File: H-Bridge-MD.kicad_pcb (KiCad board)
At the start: 2 copper layers, 85 x 50 mm, 70 parts, among them IC1 SI8650AB-B-IS1, IC2 AP7381-50SA-7, IC3 A3921KLPTR-T, IC4 SI8650AB-B-IS1, IC5 A3921KLPTR-T, J1 Conn_01x03, J2 Conn_01x05, J3 Bus_mechaken_PCIexpress_x16_1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, J4 Conn_01x02, J5 Conn_01x02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

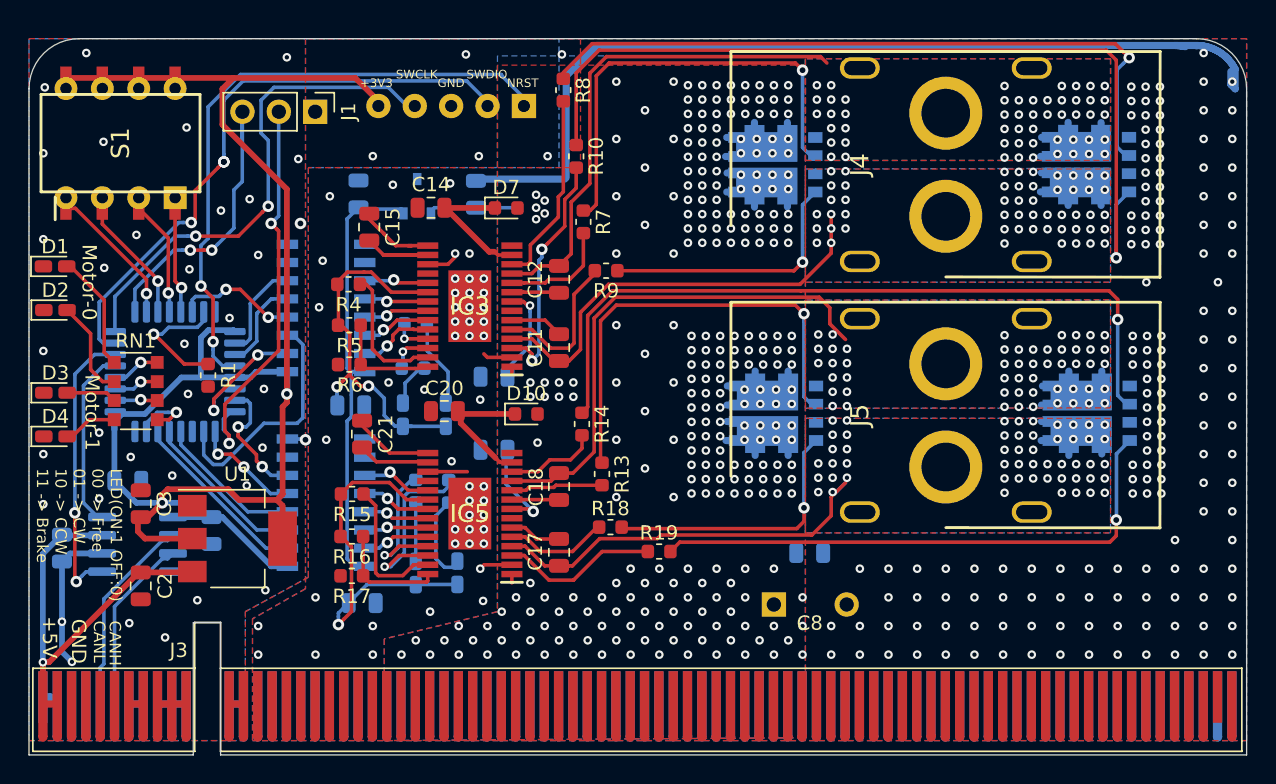
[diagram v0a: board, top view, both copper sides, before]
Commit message: change
エッジコネクタ（PCIe）を公式のライブラリを基にしたフットプリントに変更
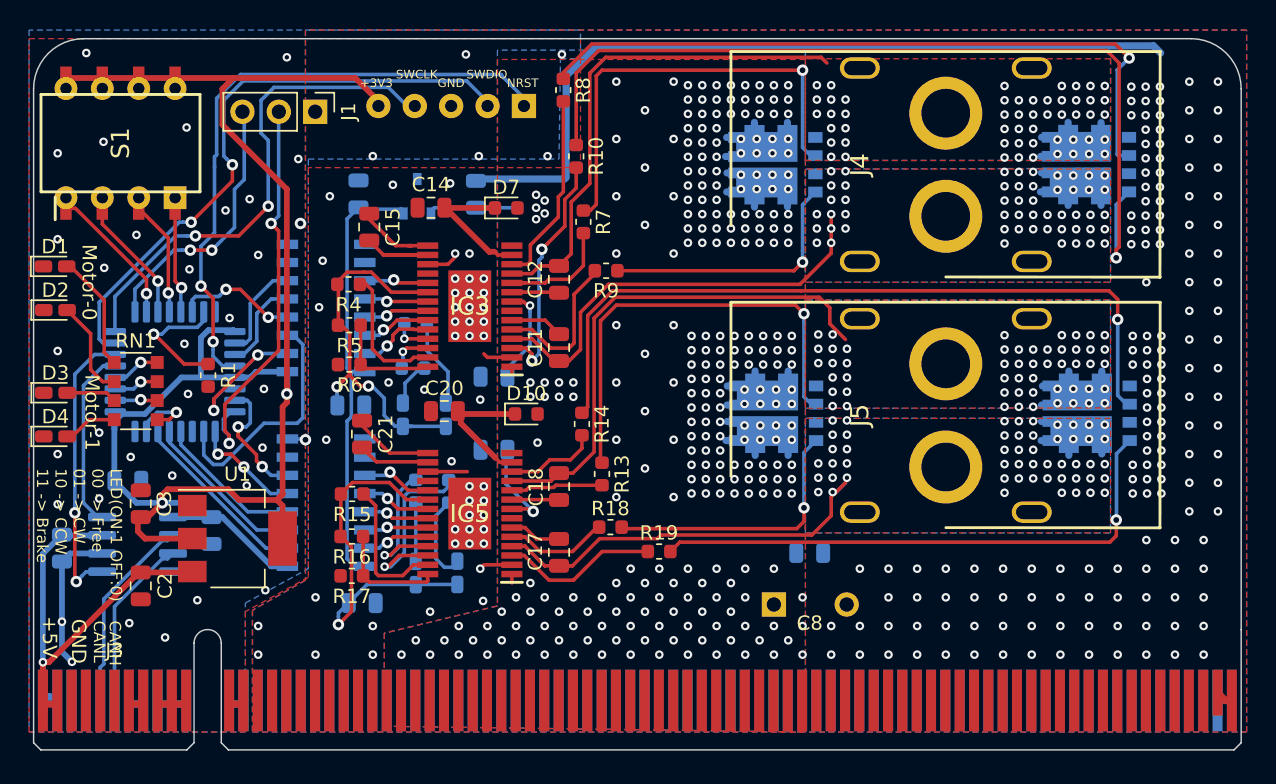
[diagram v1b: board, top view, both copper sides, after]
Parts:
- J3: footprint PCIe:BUS_mechaken_PCIexpress_x16_164_Position -> PCIe:BUS_mechaken_PCIexpress_x16
- moved J3 0.25 mm to (51.0, 86.2)
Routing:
- net GNDPWR: track 74.2 -> 67.4 mm, vias 200 -> 197
- net VCP_RX: track 20.6 -> 18.7 mm
- net /SWDIO: track 41.5 -> 42.0 mm, vias 3 -> 2
- net GND: vias 40 -> 39
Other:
- board size 85 x 50 mm -> 84.3 x 41.2 mm

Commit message: fix
細かな修正
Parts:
- moved U1 0.30 mm to (64.2, 74.9)
- moved C2 0.15 mm to (57.6, 78.2)
- moved C3 0.15 mm to (57.6, 72.5)
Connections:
- net MD_3V3 renamed VDD
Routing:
- net IC_RESET_0: track 9.81 -> 6.48 mm
- net VCP_TX: track 28.0 -> 26.0 mm
- net /SWDIO: track 42.0 -> 44.0 mm, vias 2 -> 0
- net +3V3: track 120.8 -> 122.0 mm
- net /SWCLK: track 35.2 -> 36.1 mm, vias 2 -> 0
- net IC_PHASE_1: track 8.96 -> 8.27 mm, vias 2 -> 0
- net GND: track 11.6 -> 12.3 mm, vias 39 -> 36
- net IC_SR_1: track 7.65 -> 7.01 mm, vias 2 -> 0
- net DIP_SW_2: track 9.58 -> 10.1 mm
- net VCP_RX: track 18.7 -> 19.0 mm, vias 2 -> 0
- net GNDPWR: track 67.4 -> 67.1 mm, vias 197 -> 196
- net IC_PWMH_0: track 16.6 -> 16.7 mm, vias 0 -> 2
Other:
- board text added: "Conthrough"

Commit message: clean
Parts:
- moved C3 9.28 mm to (66.6, 70.0), turned to 0 degrees
- moved R1 2.96 mm to (63.1, 60.6), turned to 0 degrees
- moved C2 2.72 mm to (55.7, 76.3), turned to 90 degrees
- moved U1 1.90 mm to (62.4, 74.9)
- moved C4 0.30 mm to (52.0, 75.6)
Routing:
- net GND: track 12.3 -> 16.1 mm, vias 36 -> 43
- net /BOOT: track 9.18 -> 5.59 mm
- net Net-(C15-Pad2): track 7.60 -> 4.50 mm
- net IC_PWML_0: track 8.41 -> 11.1 mm
- net +3V3: track 122.0 -> 119.9 mm, vias 2 -> 3
- net MD_FF1_1: track 12.9 -> 11.3 mm
- net NRST: track 44.8 -> 45.8 mm
- net IC_PWMH_0: track 16.7 -> 15.9 mm
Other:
- board text added: "Address"

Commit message: clean
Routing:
- net Net-(C14-Pad1): track 9.82 -> 10.7 mm
- net GNDPWR: track 67.1 -> 67.9 mm
- net VCC: vias 273 -> 274

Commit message: clean
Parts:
- moved IC2 0.10 mm to (77.0, 51.0)
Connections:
- net VDD renamed MD_3V3
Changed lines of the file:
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@@
     (thickness 1.6)
     (drawings 30)
-    (tracks 1519)
+    (tracks 1520)
     (zones 0)
     (modules 70)
@@
   )
   (setup
-    (last_trace_width 0.4)
+    (last_trace_width 0.25)
     (user_trace_width 0.2)
     (user_trace_width 0.4)
@@
   (net 111 "Net-(IC5-Pad27)")
   (net 112 "Net-(IC5-Pad28)")
-  (net 113 VDD)
+  (net 113 MD_3V3)
   (net_class Default "これはデフォルトのネット クラスです。"
     (clearance 0.2)
@@
     (add_net MD1_LED_H)
     (add_net MD1_LED_L)
+    (add_net MD_3V3)
     (add_net MD_FF1_0)
     (add_net MD_FF1_1)
@@
     (add_net VCP_RX)
     (add_net VCP_TX)
-    (add_net VDD)
     (add_net VREG_0)
     (add_net VREG_1)
   )
   (module SamacSys_Parts:SOT96P240X105-3N (layer B.Cu)
-    (at 77.1 51 90)
+    (at 77 51 90)
     (descr AP7381-50SA-7-1)
     (tags "Integrated Circuit")
     (attr smd)
-    (fp_text reference IC2 (at 0 0 90) (layer B.SilkS)
+    (fp_text reference IC2 (at 0 0 270) (layer B.SilkS)
       (effects (font (size 1.27 1.27) (thickness 0.254)) (justify mirror))
     )
-    (fp_text value AP7381-50SA-7 (at 0 0 90) (layer B.SilkS) hide
+    (fp_text value AP7381-50SA-7 (at 0 0 270) (layer B.SilkS) hide
       (effects (font (size 1.27 1.27) (thickness 0.254)) (justify mirror))
     )
@@
     (fp_line (start 1.875 1.75) (end 1.875 -1.75) (layer B.CrtYd) (width 0.05))
     (fp_line (start -1.875 1.75) (end 1.875 1.75) (layer B.CrtYd) (width 0.05))
-    (fp_text user %R (at 0 0 90) (layer B.Fab)
+    (fp_text user %R (at 0 0 270) (layer B.Fab)
       (effects (font (size 1.27 1.27) (thickness 0.254)) (justify mirror))
     )
@@
       (net 5 GNDPWR))
     (pad 2 smd rect (at -1.2 -0.96) (size 0.6 0.85) (layers B.Cu B.Paste B.Mask)
-      (net 113 VDD))
+      (net 113 MD_3V3))
     (pad 1 smd rect (at -1.2 0.96) (size 0.6 0.85) (layers B.Cu B.Paste B.Mask)
       (net 9 VCC))
@@
     (fp_line (start -1 -0.6) (end -1 0.6) (layer B.Fab) (width 0.1))
     (pad 2 smd roundrect (at 0.9375 0 270) (size 0.975 1.4) (layers B.Cu B.Paste B.Mask) (roundrect_rratio 0.25)
-      (net 113 VDD))
+      (net 113 MD_3V3))
     (pad 1 smd roundrect (at -0.9375 0 270) (size 0.975 1.4) (layers B.Cu B.Paste B.Mask) (roundrect_rratio 0.25)
       (net 5 GNDPWR))
@@
       (net 34 MD_RESET_0))
     (pad 16 smd rect (at 2.7 4.445 270) (size 0.65 1.5) (layers B.Cu B.Paste B.Mask)
-      (net 113 VDD))
+      (net 113 MD_3V3))
     (model C:\SamcSys_PCB_Library\KiCad\SamacSys_Parts.3dshapes\Si8651BB-B-IS1.stp
       (at (xyz 0 0 0))
@@
       (net 16 MD_RESET_1))
     (pad 16 smd rect (at 2.7 4.445 270) (size 0.65 1.5) (layers B.Cu B.Paste B.Mask)
-      (net 113 VDD))
+      (net 113 MD_3V3))
     (model C:\SamcSys_PCB_Library\KiCad\SamacSys_Parts.3dshapes\Si8651BB-B-IS1.stp
       (at (xyz 0 0 0))
@@
   (segment (start 85.6375 55.8625) (end 86.3 55.8625) (width 0.25) (layer F.Cu) (net 12))
   (segment (start 85.101 56.399) (end 85.6375 55.8625) (width 0.25) (layer F.Cu) (net 12))
-  (segment (start 89.149989 42.4136) (end 89.149989 49.581805) (width 0.25) (layer F.Cu) (net 12))
+  (segment (start 105.7 41.7) (end 105.299989 41.299989) (width 0.25) (layer F.Cu) (net 12))
   (segment (start 87.485527 55.376973) (end 87 55.8625) (width 0.25) (layer F.Cu) (net 12))
-  (segment (start 105.7 41.7) (end 105.300022 41.300022) (width 0.25) (layer F.Cu) (net 12))
-  (segment (start 90.263567 41.300022) (end 89.149989 42.4136) (width 0.25) (layer F.Cu) (net 12))
-  (segment (start 105.300022 41.300022) (end 90.263567 41.300022) (width 0.25) (layer F.Cu) (net 12))
-  (segment (start 89.149989 49.581805) (end 87.849989 50.881805) (width 0.25) (layer F.Cu) (net 12))
+  (segment (start 90.2636 41.299989) (end 89.149989 42.4136) (width 0.25) (layer F.Cu) (net 12))
   (segment (start 87.849989 50.881805) (end 87.849989 55.012511) (width 0.25) (layer F.Cu) (net 12))
+  (segment (start 89.149989 49.581805) (end 87.849989 50.881805) (width 0.25) (layer F.Cu) (net 12))
   (segment (start 87.849989 55.012511) (end 87.485527 55.376973) (width 0.25) (layer F.Cu) (net 12))
+  (segment (start 105.299989 41.299989) (end 90.2636 41.299989) (width 0.25) (layer F.Cu) (net 12))
+  (segment (start 89.149989 42.4136) (end 89.149989 49.581805) (width 0.25) (layer F.Cu) (net 12))
   (segment (start 55.25 61.9) (end 55.95 62.6) (width 0.25) (layer F.Cu) (net 13))
   (segment (start 55.25 58.25) (end 55.25 61.9) (width 0.25) (layer F.Cu) (net 13))
@@
   (segment (start 104.892 48.165) (end 104.565 48.165) (width 0.25) (layer B.Cu) (net 49))
   (segment (start 104.565 48.165) (end 104 47.6) (width 0.25) (layer B.Cu) (net 49))
-  (segment (start 89.6 49.9) (end 89.6 42.6) (width 0.25) (layer F.Cu) (net 49))
+  (segment (start 90.45 41.75) (end 103.55 41.75) (width 0.25) (layer F.Cu) (net 49))
   (segment (start 88.7 52) (end 88.7 50.8) (width 0.25) (layer F.Cu) (net 49))
-  (segment (start 90 42.2) (end 104 42.2) (width 0.25) (layer F.Cu) (net 49))
-  (segment (start 89.6 42.6) (end 90 42.2) (width 0.25) (layer F.Cu) (net 49))
+  (segment (start 103.55 41.75) (end 104 42.2) (width 0.25) (layer F.Cu) (net 49))
+  (segment (start 89.6 49.9) (end 89.6 42.6) (width 0.25) (layer F.Cu) (net 49))
+  (segment (start 89.6 42.6) (end 90.45 41.75) (width 0.25) (layer F.Cu) (net 49))
   (segment (start 88.7 50.8) (end 89.6 49.9) (width 0.25) (layer F.Cu) (net 49))
   (via (at 125.9 55.3) (size 0.8) (drill 0.4) (layers F.Cu B.Cu) (net 50))
